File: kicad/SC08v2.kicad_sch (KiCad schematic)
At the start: 21 parts, among them J2 USB_C_Receptacle_PowerOnly_6P

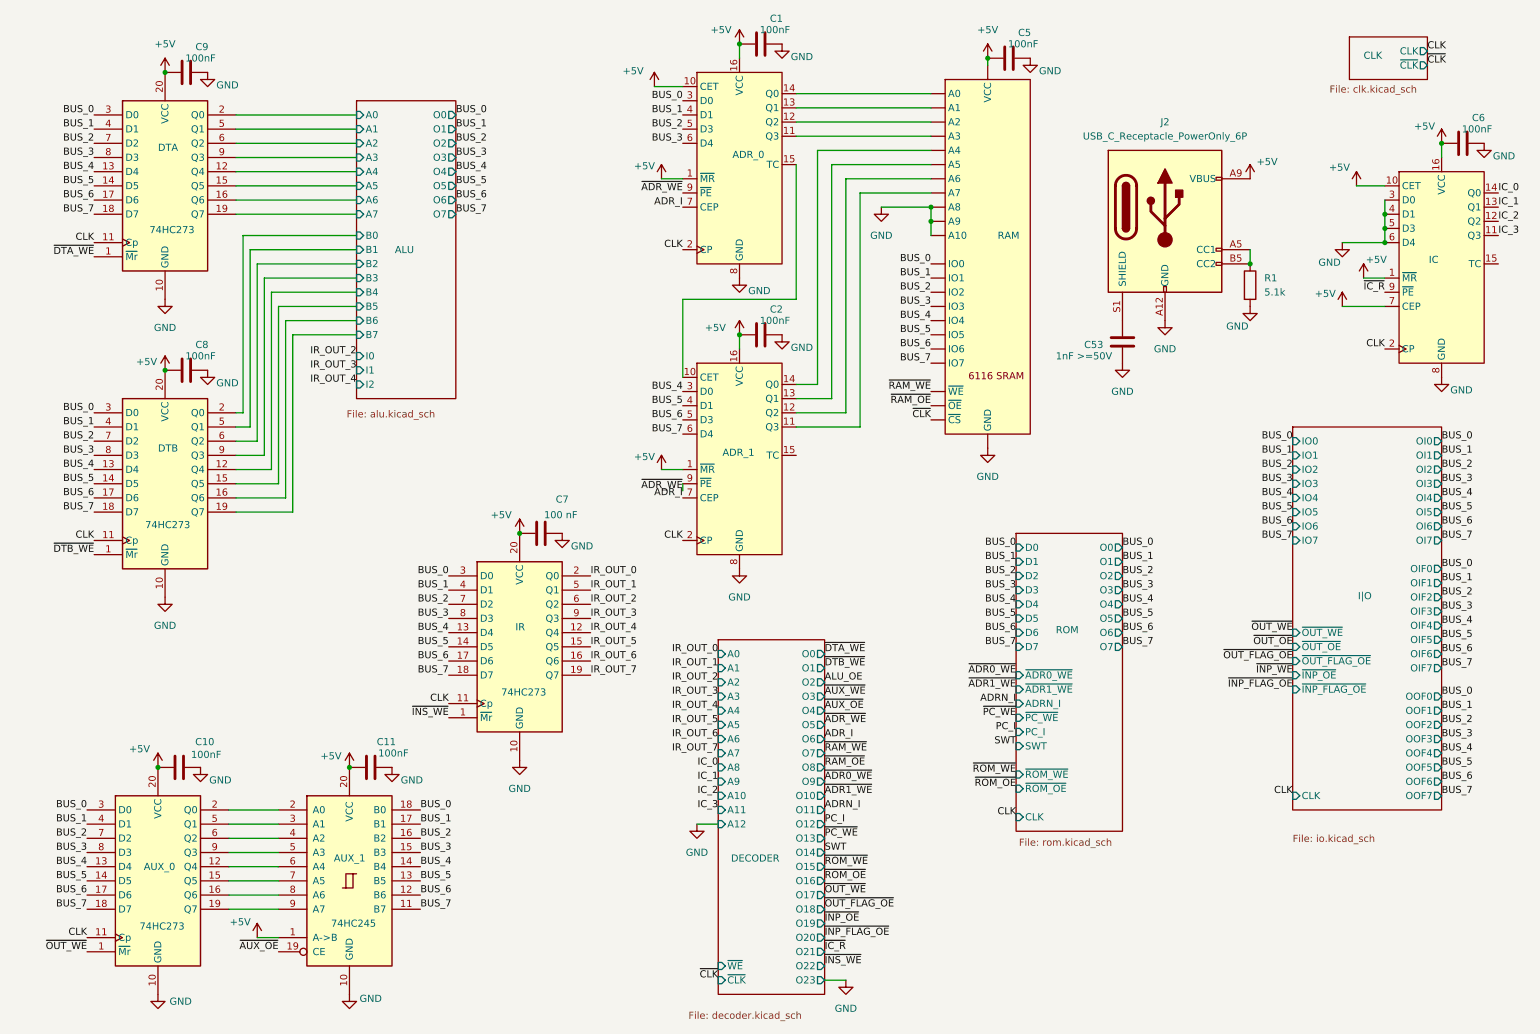
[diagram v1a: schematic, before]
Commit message: kicad: compact design
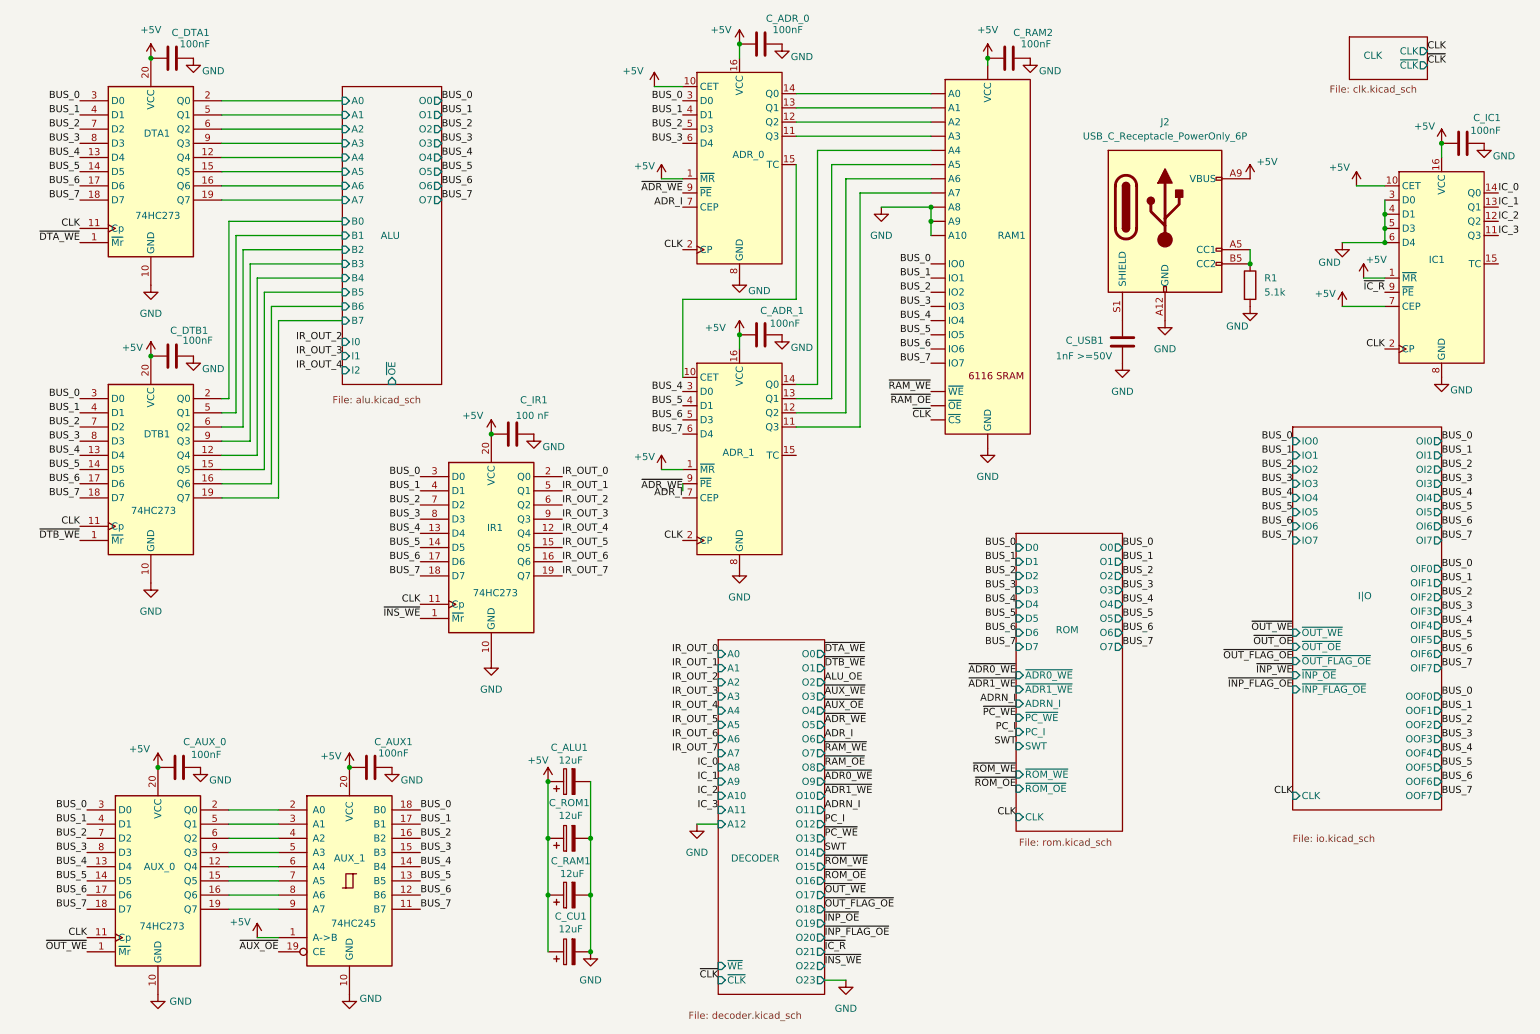
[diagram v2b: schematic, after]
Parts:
- added C_ALU1, C_CU1, C_RAM1, C_ROM1: 12uF, symbol Device:C_Polarized
- renumbered C1 to C_ADR_0, C2 to C_ADR_1, C11 to C_AUX1, C10 to C_AUX_0, C9 to C_DTA1, C8 to C_DTB1, C6 to C_IC1, C7 to C_IR1, C5 to C_RAM2, C53 to C_USB1, DTA to DTA1, DTB to DTB1, IC to IC1, IR to IR1, RAM to RAM1
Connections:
- net +5V: now also C_ALU1.1, C_CU1.1, C_RAM1.1, C_ROM1.1
- net GND: now also C_ALU1.2, C_CU1.2, C_RAM1.2, C_ROM1.2
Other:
- sheet ALU ports: added ~{OE}; removed none
- moved on the sheet: C_DTA1, C_DTB1, C_IR1, DTA1, DTB1, IR1

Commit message: kicad: finalize sketch
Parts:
- ADR0_U0: renamed from ADR_0; footprint (none) -> Package_DIP:DIP-16_W7.62mm
- ADR0_U0_C1: renamed from C_ADR_0; footprint (none) -> Capacitor_THT:C_Disc_D3.0mm_W1.6mm_P2.50mm
- ADR0_U1: renamed from ADR_1; footprint (none) -> Package_DIP:DIP-16_W7.62mm
- ADR0_U1_C1: renamed from C_ADR_1; footprint (none) -> Capacitor_THT:C_Disc_D3.0mm_W1.6mm_P2.50mm
- ALU_C1: renamed from C_ALU1; footprint (none) -> Capacitor_THT:C_Radial_D5.0mm_H5.0mm_P2.00mm
- AUX_U0_C1: renamed from C_AUX_0; footprint (none) -> Capacitor_THT:C_Disc_D3.0mm_W1.6mm_P2.50mm
- AUX_U1: renamed from AUX_1; footprint (none) -> Package_DIP:DIP-20_W7.62mm
- AUX_U1_C1: renamed from C_AUX1; footprint (none) -> Capacitor_THT:C_Disc_D3.0mm_W1.6mm_P2.50mm
- CU_C1: renamed from C_CU1; footprint (none) -> Capacitor_THT:C_Radial_D5.0mm_H5.0mm_P2.00mm
- DTA_U_C1: renamed from C_DTA1; footprint (none) -> Capacitor_THT:C_Disc_D3.0mm_W1.6mm_P2.50mm
- DTB_U_C1: renamed from C_DTB1; footprint (none) -> Capacitor_THT:C_Disc_D3.0mm_W1.6mm_P2.50mm
- IC_U1: renamed from IC1; footprint (none) -> Package_DIP:DIP-16_W7.62mm
- IC_U_C1: renamed from C_IC1; footprint (none) -> Capacitor_THT:C_Disc_D3.0mm_W1.6mm_P2.50mm
- IR_U_C1: renamed from C_IR1; footprint (none) -> Capacitor_THT:C_Disc_D3.0mm_W1.6mm_P2.50mm
- RAM_C1: renamed from C_RAM1; footprint (none) -> Capacitor_THT:C_Radial_D5.0mm_H5.0mm_P2.00mm
- RAM_U1: renamed from RAM1; footprint (none) -> Package_DIP:DIP-24_18.0mmx34.29mm_W15.24mm
- RAM_U_C1: renamed from C_RAM2; footprint (none) -> Capacitor_THT:C_Disc_D3.0mm_W1.6mm_P2.50mm
- ROM_C1: renamed from C_ROM1; footprint (none) -> Capacitor_THT:C_Radial_D5.0mm_H5.0mm_P2.00mm
- USB_CONN1: renamed from J2; footprint (none) -> Connector_USB:USB_C_Receptacle_GCT_USB4125-xx-x-0190_6P_TopMnt_Horizontal
- USB_CONN_C1: renamed from C_USB1; footprint (none) -> Capacitor_THT:C_Disc_D3.0mm_W1.6mm_P2.50mm
- USB_CONN_R1: renamed from R1; footprint (none) -> Resistor_THT:R_Axial_DIN0204_L3.6mm_D1.6mm_P5.08mm_Horizontal
- renumbered AUX_0 to AUX_U0, DTA1 to DTA_U1, DTB1 to DTB_U1, IR1 to IR_U1
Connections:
- net ~{ADR_WE} is gone; now on net ~{ADR0_WE}: ADR0_U0.9 (~{PE}), ADR0_U1.9 (~{PE})
- net +5V: now also RAM_U1.24 (VCC); no longer RAM_U1. (GND)
- net BUS_0: now also RAM_U1.9 (IO0); no longer RAM_U1. (GND)
- net BUS_1: now also RAM_U1.10 (IO1); no longer RAM_U1. (GND)
- net BUS_2: now also RAM_U1.11 (IO2); no longer RAM_U1. (GND)
- net BUS_3: now also RAM_U1.13 (IO3); no longer RAM_U1. (GND)
- net BUS_4: now also RAM_U1.14 (IO4); no longer RAM_U1. (GND)
- net BUS_5: now also RAM_U1.15 (IO5); no longer RAM_U1. (GND)
- net BUS_6: now also RAM_U1.16 (IO6); no longer RAM_U1. (GND)
- net BUS_7: now also RAM_U1.17 (IO7); no longer RAM_U1. (GND)
- net GND: now also RAM_U1.12 (GND), RAM_U1.19 (A10), RAM_U1.22 (A9), RAM_U1.23 (A8); no longer RAM_U1. (GND)
- net ~{CLK}: now also RAM_U1.18 (~{CS}); no longer RAM_U1. (GND)
- net ~{RAM_OE}: now also RAM_U1.20 (~{OE}); no longer RAM_U1. (GND)
- net ~{RAM_WE}: now also RAM_U1.21 (~{WE}); no longer RAM_U1. (GND)
- net at ADR0_U0.11 (Q3): now also RAM_U1.5 (A3); no longer RAM_U1. (GND)
- net at ADR0_U0.12 (Q2): now also RAM_U1.6 (A2); no longer RAM_U1. (GND)
- net at ADR0_U0.13 (Q1): now also RAM_U1.7 (A1); no longer RAM_U1. (GND)
- net at ADR0_U0.14 (Q0): now also RAM_U1.8 (A0); no longer RAM_U1. (GND)
- net at ADR0_U1.11 (Q3): now also RAM_U1.1 (A7); no longer RAM_U1. (GND)
- net at ADR0_U1.12 (Q2): now also RAM_U1.2 (A6); no longer RAM_U1. (GND)
- net at ADR0_U1.13 (Q1): now also RAM_U1.3 (A5); no longer RAM_U1. (GND)
- net at ADR0_U1.14 (Q0): now also RAM_U1.4 (A4); no longer RAM_U1. (GND)
- net ADR_I renamed ADR0_I
- no-connect marks 0 -> 2
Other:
- sheet DECODER ports: added none; removed ~{WE}
- sheet ROM ports: added ADR12_I, ~{ADR2_WE}; removed ADRN_I, ~{ADR0_WE}
